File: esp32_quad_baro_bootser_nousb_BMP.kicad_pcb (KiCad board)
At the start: 2 copper layers, 45 x 45 mm, 68 parts, among them J1 Conn_01x02_Pin, J2 Conn_01x02_Female, J4 Conn_01x02_Female, J5 Conn_01x02_Female, J6 Conn_01x02_Female, J8 Conn_01x06_Female, J9 Conn_01x06_Female, SW1 K3-1280S-F1, T1 SI2302DS-T1, T2 SI2302DS-T1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

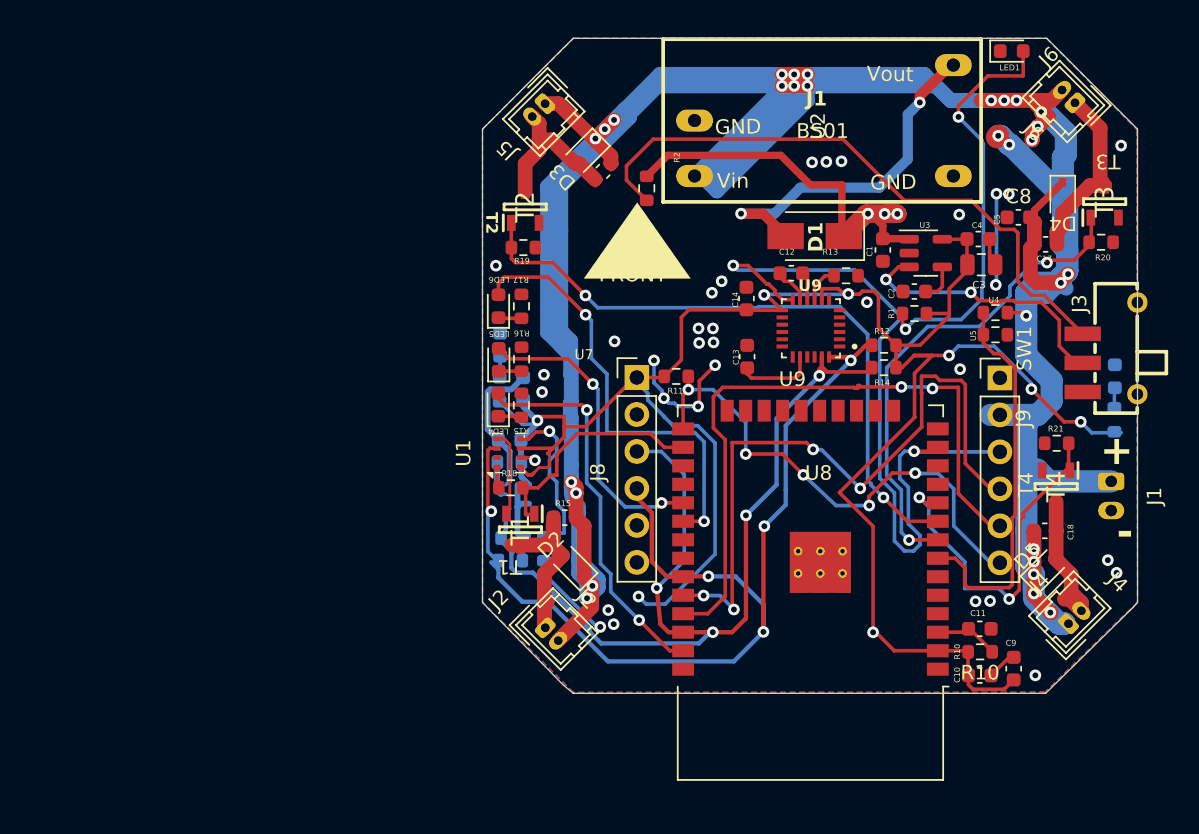
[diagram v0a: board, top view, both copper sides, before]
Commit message: CHANGED WIRE THICKNESS
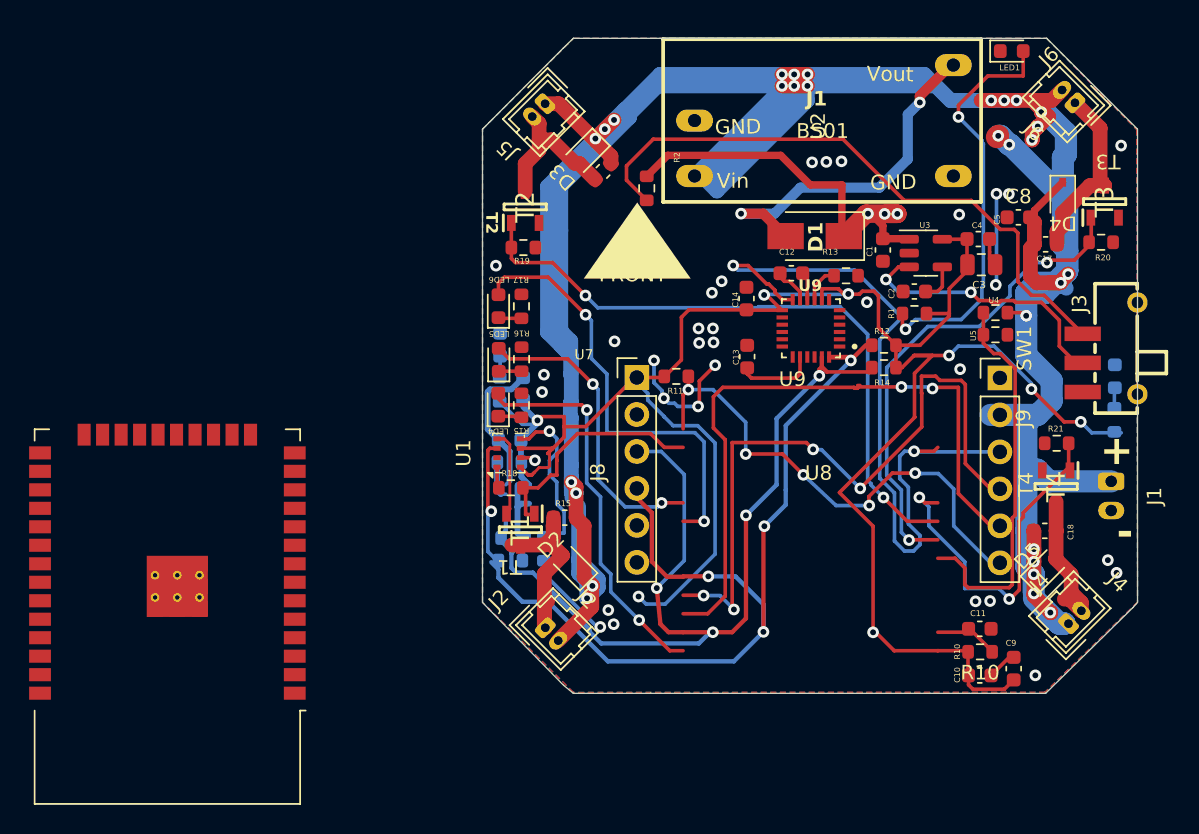
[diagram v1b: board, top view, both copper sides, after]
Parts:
- moved U8 44.2 mm to (86.8, 100.8)
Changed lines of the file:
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@@
 			(psa4output no)
 			(plot_black_and_white yes)
-			(plotinvisibletext no)
 			(sketchpadsonfab no)
 			(plotpadnumbers no)
@@
 	(footprint "RF_Module:ESP32-WROOM-32"
 		(layer "F.Cu")
-		(at 130.92811 99.10145 180)
+		(at 86.7501 100.7501 180)
 		(descr "Single 2.4 GHz Wi-Fi and Bluetooth combo chip https://www.espressif.com/sites/default/files/documentation/esp32-wroom-32_datasheet_en.pdf")
 		(tags "Single 2.4 GHz Wi-Fi and Bluetooth combo  chip")
@@
 			(polygon
 				(pts
-					(xy 140.12291 108.90585) (xy 121.73331 108.90585) (xy 121.73331 115.02725) (xy 140.12291 115.02725)
+					(xy 95.9449 110.5545) (xy 77.5553 110.5545) (xy 77.5553 116.6759) (xy 95.9449 116.6759)
 				)
 			)

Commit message: PCB
C:\Users\Robo\Downloads\New folder (2)\OUTPUT
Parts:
- moved U8 44.2 mm to (130.9, 99.1)
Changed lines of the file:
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@@
 			(plot_on_all_layers_selection 0x00000000_00000000_00000000_02000000)
 			(disableapertmacros no)
-			(usegerberextensions no)
-			(usegerberattributes yes)
-			(usegerberadvancedattributes yes)
-			(creategerberjobfile yes)
+			(usegerberextensions yes)
+			(usegerberattributes no)
+			(usegerberadvancedattributes no)
+			(creategerberjobfile no)
 			(dashed_line_dash_ratio 12.000000)
 			(dashed_line_gap_ratio 3.000000)
@@
 			(drillshape 0)
 			(scaleselection 1)
-			(outputdirectory "garber/")
+			(outputdirectory "../../../Downloads/New folder (2)/OUTPUT/")
 		)
 	)
@@
 	(footprint "RF_Module:ESP32-WROOM-32"
 		(layer "F.Cu")
-		(at 86.7501 100.7501 180)
+		(at 130.92811 99.10145 180)
 		(descr "Single 2.4 GHz Wi-Fi and Bluetooth combo chip https://www.espressif.com/sites/default/files/documentation/esp32-wroom-32_datasheet_en.pdf")
 		(tags "Single 2.4 GHz Wi-Fi and Bluetooth combo  chip")
@@
 			(polygon
 				(pts
-					(xy 95.9449 110.5545) (xy 77.5553 110.5545) (xy 77.5553 116.6759) (xy 95.9449 116.6759)
+					(xy 140.12291 108.90585) (xy 121.73331 108.90585) (xy 121.73331 115.02725) (xy 140.12291 115.02725)
 				)
 			)
